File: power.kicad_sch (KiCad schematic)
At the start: 49 parts, among them J11 Conn_01x02_Pin, J14 Conn_01x02_Pin, J8 Conn_01x02_Pin, U10 MAX4995AAUT+T, U11 MAX4995AAUT+T, U35 MAX4995AAUT+T, U4 TPSM828302ARDSR, U5 SN74AHC1G00QDCKRQ1, U6 STWD100NYWY3F, U8 MP5073GG-P, U9 MAX4995AAUT+T

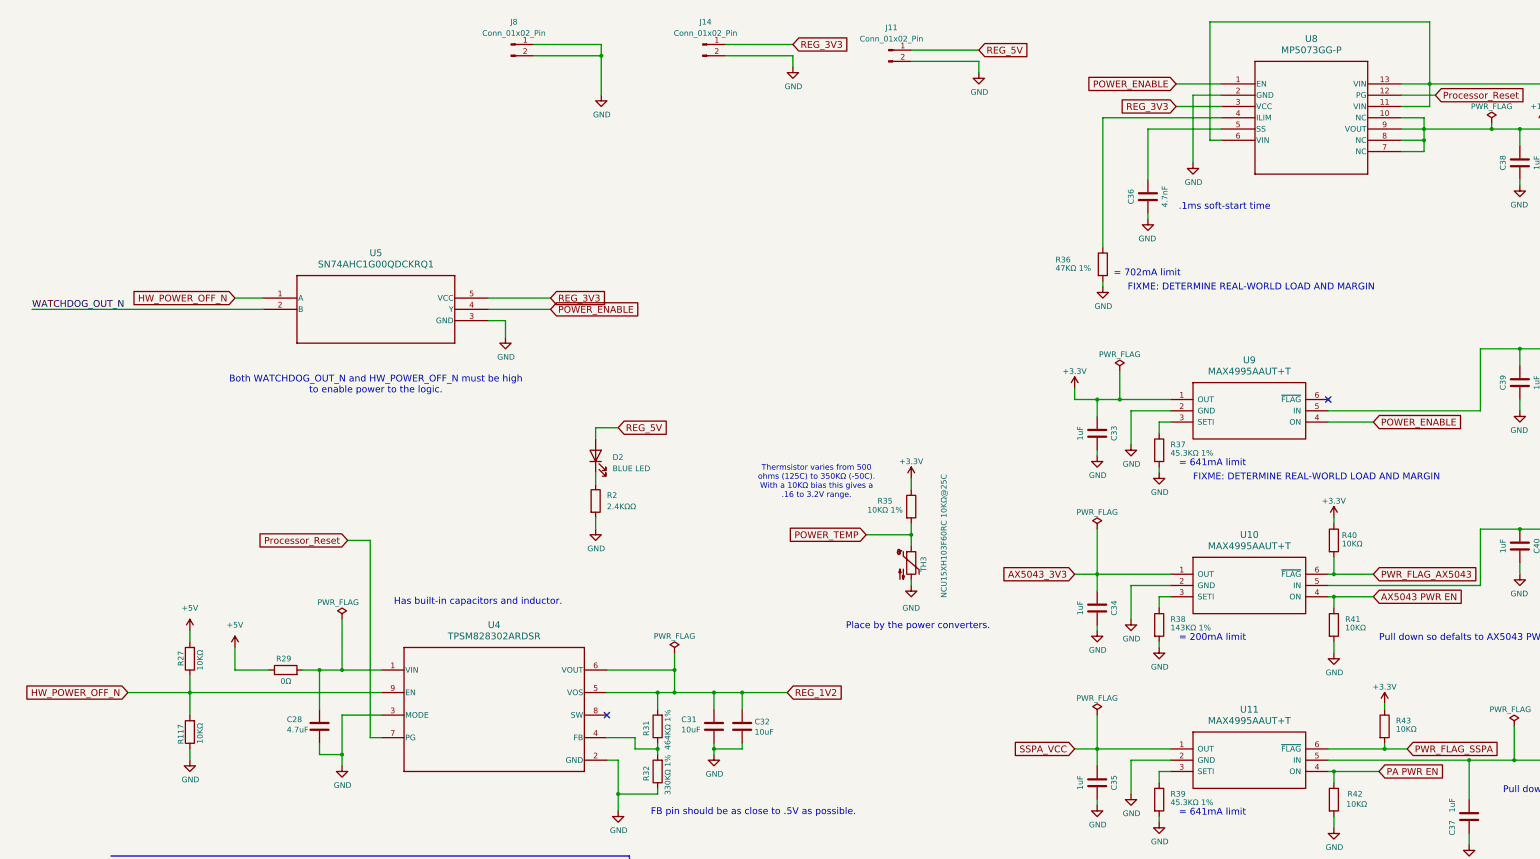
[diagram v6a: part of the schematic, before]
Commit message: Add an UMBILICAL_ATTACHED signal from the PC104
Allow the board to know if it is in the launch vehicle.  Will
hardware inhibit transmit.

Signed-off-by: Corey Minyard <corey@minyard.net>
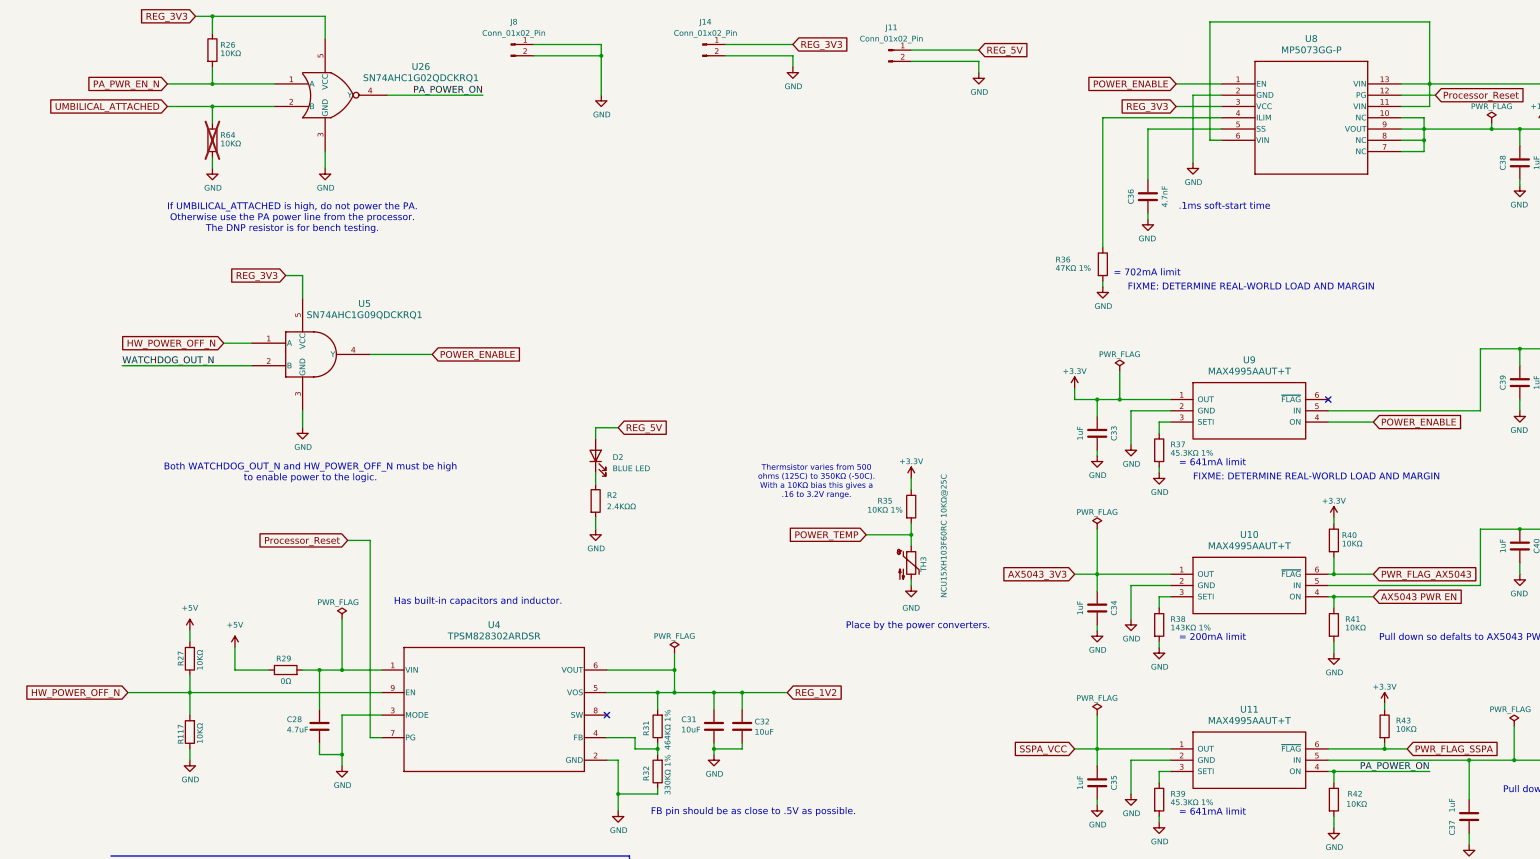
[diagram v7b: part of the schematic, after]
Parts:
- added R26, R64: 10KΩ, Resistor_SMD:R_0402_1005Metric_Pad0.72x0.64mm_HandSolder, symbol Device:R
- added U26: SN74AHC1G02QDCKRQ1, PacSatDev_ti:DCK5, symbol PACSAT_ICs:SN74AHC1G02QDCKRQ1
- U5: value SN74AHC1G00QDCKRQ1 -> SN74AHC1G09QDCKRQ1; symbol PACSAT_ICs:SN74AHC1G00QDCKRQ1 -> PACSAT_ICs:SN74AHC1G09QDCKRQ1
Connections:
- net GND: now also R64.2, U26.3 (GND)
- net REG_3V3: now also R26.1, U26.5 (VCC)
- net PA PWR EN renamed PA_POWER_ON
- net PA_POWER_ON: now also U26.4 (Y)
- new net PA_PWR_EN_N: R26.2, U26.1 (A)
- new net UMBILICAL_ATTACHED: R64.1, U26.2 (B)
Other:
- note added: "If UMBILICAL_ATTACHED is high, do not power the PA. Otherwise use the PA power line from the processor. The DNP resistor is for bench testing."
- moved on the sheet: U5

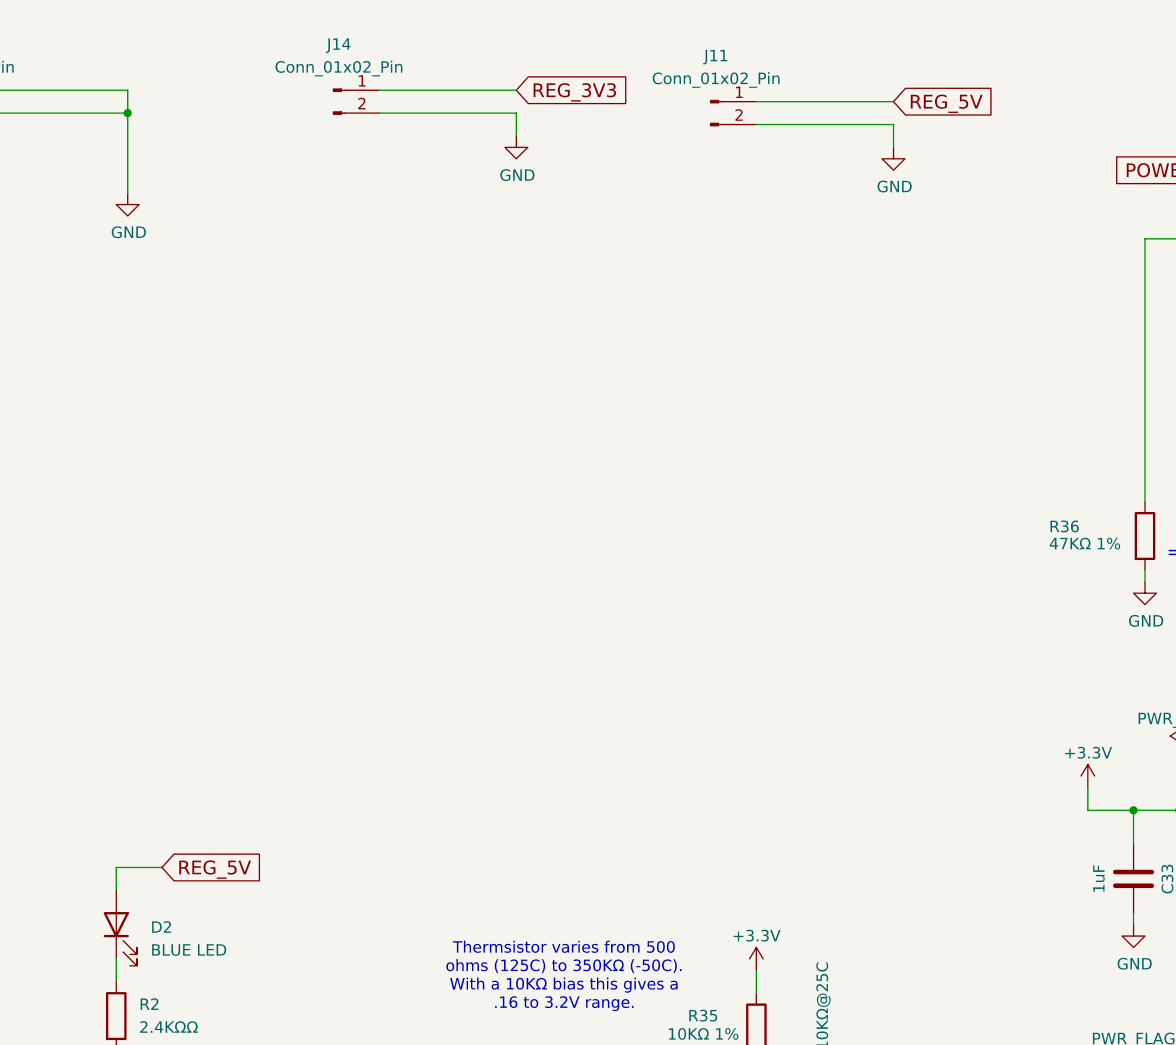
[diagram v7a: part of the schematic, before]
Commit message: Move 3.3V bench input to the other side of the inductor
Signed-off-by: Corey Minyard <corey@minyard.net>
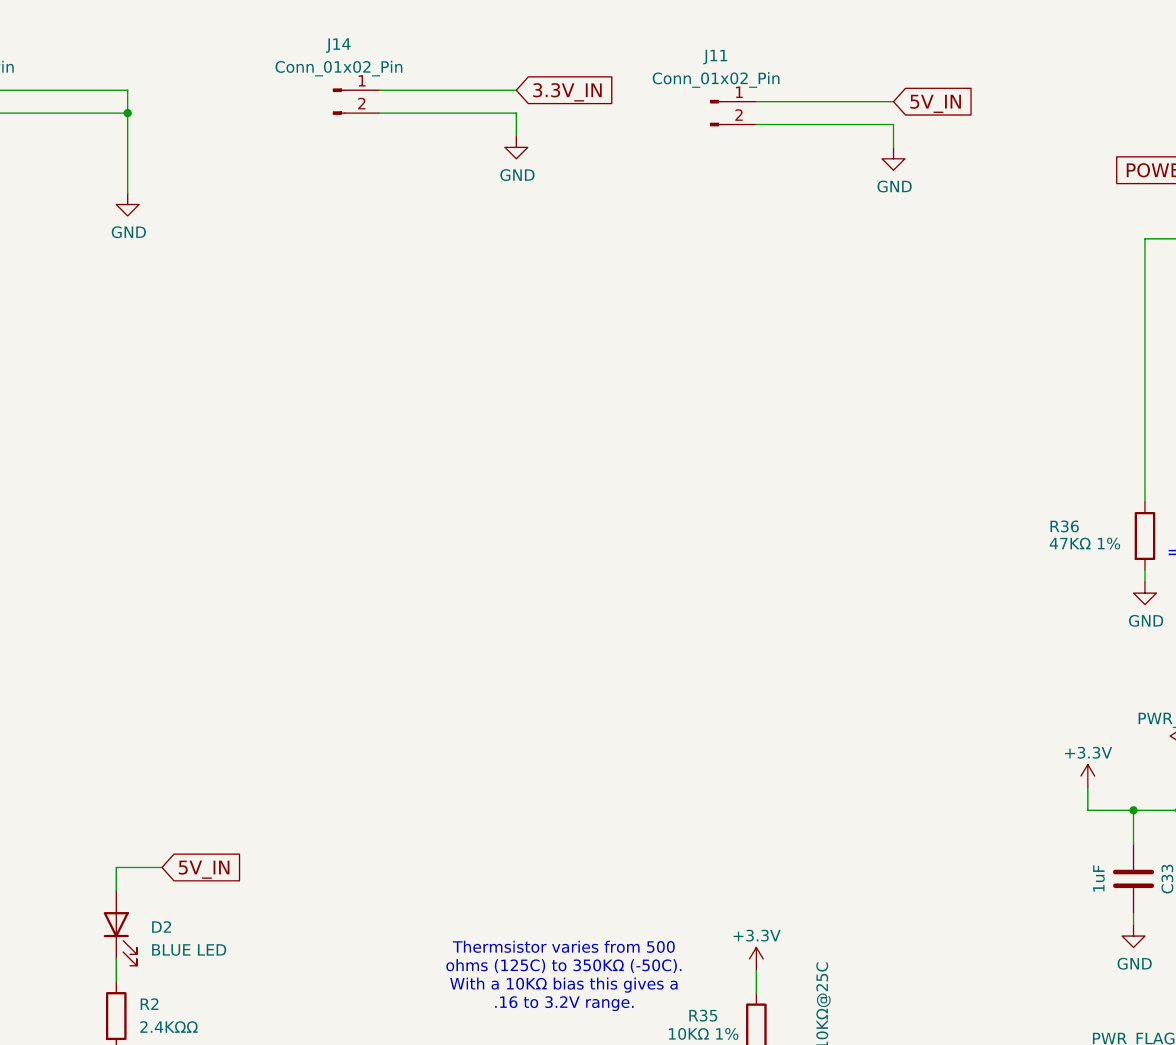
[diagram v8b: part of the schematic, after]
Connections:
- net REG_3V3: no longer J14.1 (Pin_1)
- net REG_5V renamed 5V_IN
- new net 3.3V_IN: J14.1 (Pin_1)
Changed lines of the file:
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@@
 		)
 	)
-	(global_label "REG_5V"
+	(global_label "5V_IN"
 		(shape input)
 		(at 246.38 26.67 0)
@@
 		)
 	)
-	(global_label "REG_5V"
+	(global_label "5V_IN"
 		(shape input)
 		(at 165.1 111.76 0)
@@
 		)
 	)
-	(global_label "REG_3V3"
+	(global_label "3.3V_IN"
 		(shape input)
 		(at 204.47 25.4 0)
@@
 		)
 		(property "Intersheetrefs" "${INTERSHEET_REFS}"
-			(at 217.0639 25.4 0)
-			(effects
-				(font
+			(at 215.685 25.4 0)
+			(effects
+				(font
